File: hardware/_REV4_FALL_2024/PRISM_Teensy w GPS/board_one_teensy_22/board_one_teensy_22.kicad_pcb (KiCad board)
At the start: 2 copper layers, 61 x 88.9 mm, 33 parts, among them J1 Micro_SD_Card_Det_Hirose_DM3AT, J3 3387, Q1 AO3400A, Q2 AO3400A, U1 Teensy4.0, U2 GPS-14414, U3 3966, U4 RFM69HCW_Breakout, U5 CT25E-16T150-1, U6 CMI-9605-1280T

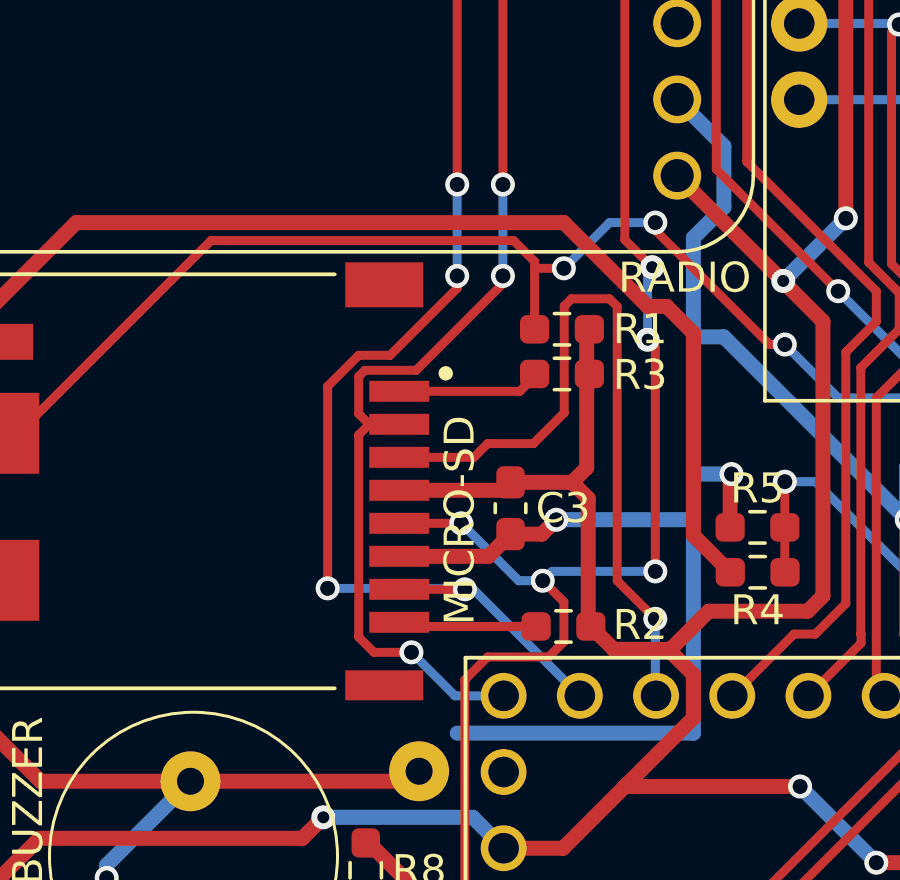
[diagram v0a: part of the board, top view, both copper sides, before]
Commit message: Fixed PRISM SD Card
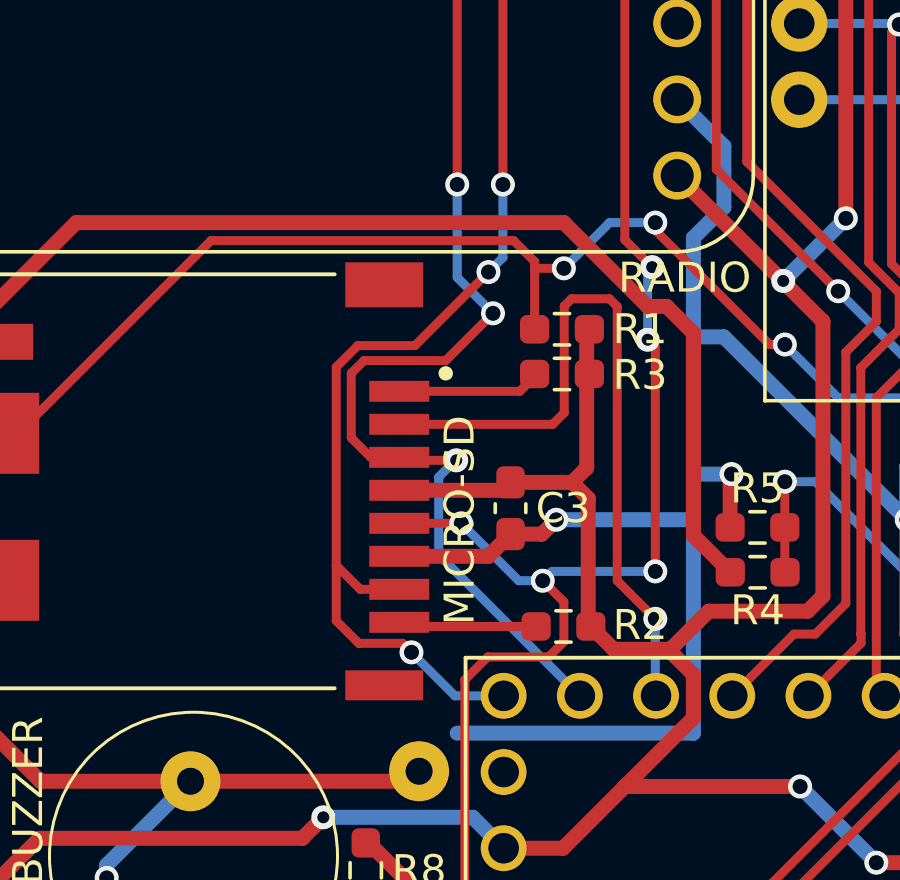
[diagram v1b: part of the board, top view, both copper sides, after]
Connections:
- J1 pad 2: /MISO -> /SD_CS
- J1 pad 3: /SD_CS -> /MOSI
- J1 pad 7: /MOSI -> /MISO
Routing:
- net /MISO: track 42.0 -> 44.0 mm
- net /MOSI: track 48.3 -> 46.7 mm, vias 4 -> 3
